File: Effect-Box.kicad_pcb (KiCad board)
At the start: 6 copper layers, 178.6 x 140 mm, 161 parts, among them J1 Conn_02x07_Odd_Even, J10 Power pins, J2 26642801RP2, J3 FH12A-10S-0.5SH55, J5 Conn_ARM_JTAG_SWD_20, J6 26642801RP2, J7 AudioJack3, J8 AudioJack3, J9 PJ-006A-SMT, SW0 SW_Push, SW1 SW_Push, SW2 SW_Push, SW3 SW_Push, SW4 SW_Push, SW5 SW_Push, SW6 SW_Push, U1 TPS54325, U10 LM7805SX_NOPB, U2 TPS54294, U3 XC7A100T-FTG256, U4 S25FL1, U5 SiT2024B, U7 EFM32GG942F1024, U8 INA1651IPW, U9 PCM3003E

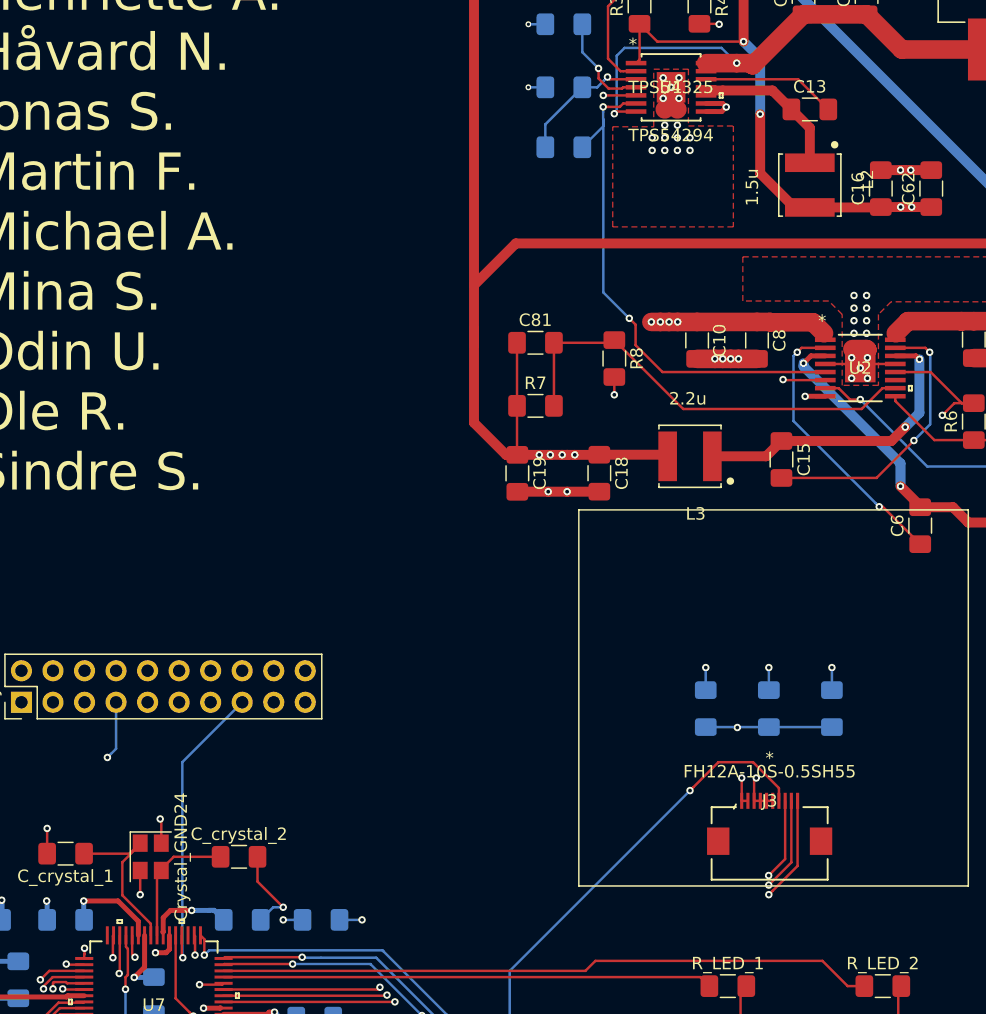
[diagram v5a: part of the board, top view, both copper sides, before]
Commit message: Fix more silkscreen and reimport from schematic
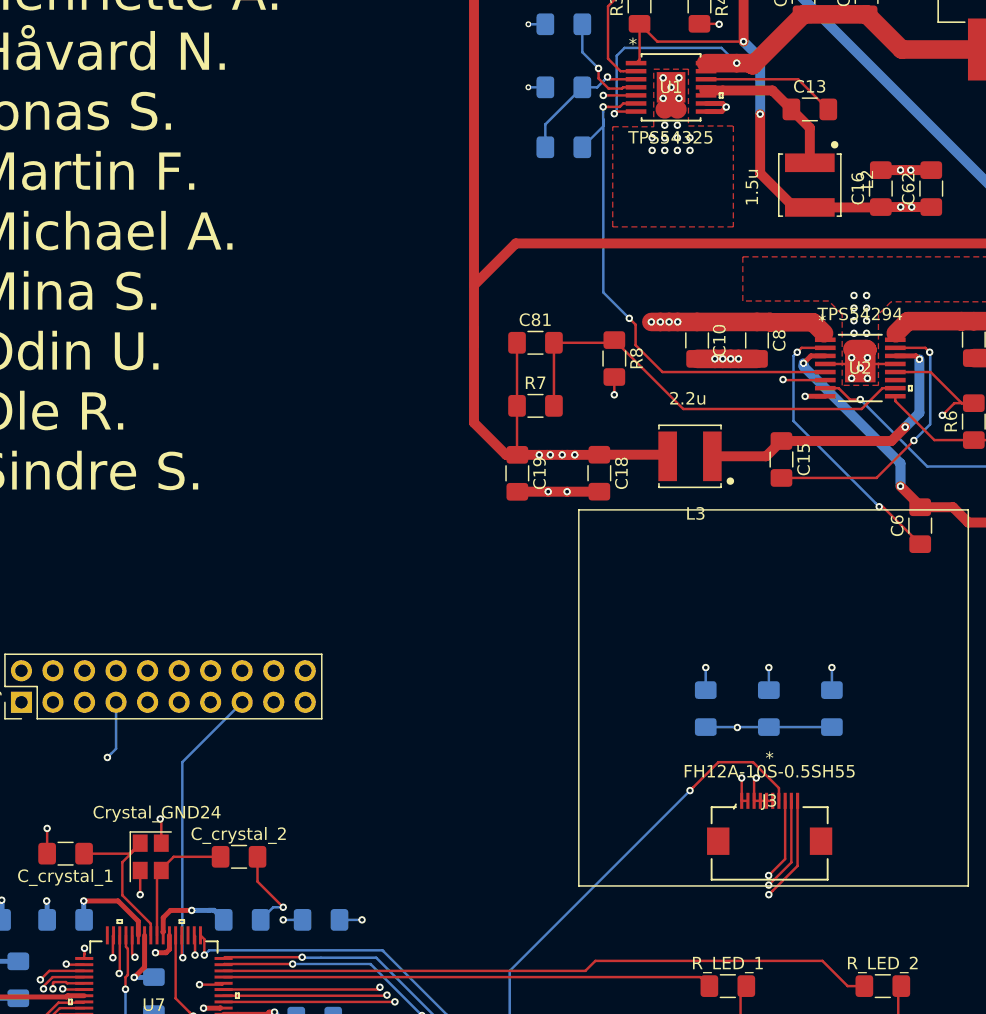
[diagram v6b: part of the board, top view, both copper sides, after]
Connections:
- J1 pad 12: (no net) -> Net-(J1-Pad12)
- J1 pad 14: (no net) -> Net-(J1-Pad14)
- J2 pad 17: (no net) -> Net-(J2-Pad17)
- J2 pad 18: (no net) -> Net-(J2-Pad18)
- J2 pad 19: (no net) -> Net-(J2-Pad19)
- J2 pad 20: (no net) -> Net-(J2-Pad20)
- J2 pad 21: (no net) -> Net-(J2-Pad21)
- J2 pad 22: (no net) -> Net-(J2-Pad22)
- J2 pad 23: (no net) -> Net-(J2-Pad23)
- J2 pad 24: (no net) -> Net-(J2-Pad24)
- J2 pad 25: (no net) -> Net-(J2-Pad25)
- J2 pad 26: (no net) -> Net-(J2-Pad26)
- J3 pad 11: (no net) -> Net-(J3-Pad11)
- J3 pad 12: (no net) -> Net-(J3-Pad12)
- J5 pad 11: (no net) -> Net-(J5-Pad11)
- J5 pad 17: (no net) -> Net-(J5-Pad17)
- J5 pad 19: (no net) -> Net-(J5-Pad19)
- J5 pad 2: (no net) -> Net-(J5-Pad2)
- J5 pad 3: (no net) -> Net-(J5-Pad3)
- J5 pad 5: (no net) -> Net-(J5-Pad5)
- J9 pad 3: (no net) -> Net-(J9-Pad3)
- U2 pad 11: (no net) -> Net-(U2-Pad11)
- U3 pad A10: (no net) -> Net-(U3-PadA10)
- U3 pad A12: (no net) -> Net-(U3-PadA12)
- U3 pad A13: (no net) -> Net-(U3-PadA13)
- U3 pad A14: (no net) -> Net-(U3-PadA14)
- U3 pad A15: (no net) -> Net-(U3-PadA15)
- U3 pad A2: (no net) -> Net-(U3-PadA2)
- U3 pad A3: (no net) -> Net-(U3-PadA3)
- U3 pad A4: (no net) -> Net-(U3-PadA4)
- U3 pad A5: (no net) -> Net-(U3-PadA5)
- U3 pad A7: (no net) -> Net-(U3-PadA7)
- U3 pad A8: (no net) -> Net-(U3-PadA8)
- U3 pad A9: (no net) -> Net-(U3-PadA9)
- U3 pad B1: (no net) -> Net-(U3-PadB1)
- U3 pad B10: (no net) -> Net-(U3-PadB10)
- U3 pad B11: (no net) -> Net-(U3-PadB11)
- U3 pad B12: (no net) -> Net-(U3-PadB12)
- U3 pad B14: (no net) -> Net-(U3-PadB14)
- U3 pad B15: (no net) -> Net-(U3-PadB15)
- U3 pad B16: (no net) -> Net-(U3-PadB16)
- U3 pad B2: (no net) -> Net-(U3-PadB2)
- U3 pad B4: (no net) -> Net-(U3-PadB4)
- U3 pad B5: (no net) -> Net-(U3-PadB5)
- U3 pad B6: (no net) -> Net-(U3-PadB6)
- U3 pad B7: (no net) -> Net-(U3-PadB7)
- U3 pad B9: (no net) -> Net-(U3-PadB9)
- U3 pad C1: (no net) -> Net-(U3-PadC1)
- U3 pad C11: (no net) -> Net-(U3-PadC11)
- U3 pad C12: (no net) -> Net-(U3-PadC12)
- U3 pad C13: (no net) -> Net-(U3-PadC13)
- U3 pad C14: (no net) -> Net-(U3-PadC14)
- U3 pad C16: (no net) -> Net-(U3-PadC16)
- U3 pad C2: (no net) -> Net-(U3-PadC2)
- U3 pad C3: (no net) -> Net-(U3-PadC3)
- U3 pad C4: (no net) -> Net-(U3-PadC4)
- U3 pad C6: (no net) -> Net-(U3-PadC6)
- U3 pad C7: (no net) -> Net-(U3-PadC7)
- U3 pad C8: (no net) -> Net-(U3-PadC8)
- U3 pad C9: (no net) -> Net-(U3-PadC9)
- U3 pad D1: (no net) -> Net-(U3-PadD1)
- U3 pad D10: (no net) -> Net-(U3-PadD10)
- U3 pad D11: (no net) -> Net-(U3-PadD11)
- U3 pad D13: (no net) -> Net-(U3-PadD13)
- U3 pad D14: (no net) -> Net-(U3-PadD14)
- U3 pad D15: (no net) -> Net-(U3-PadD15)
- U3 pad D16: (no net) -> Net-(U3-PadD16)
- U3 pad D3: (no net) -> Net-(U3-PadD3)
- U3 pad D4: (no net) -> Net-(U3-PadD4)
- U3 pad D5: (no net) -> Net-(U3-PadD5)
- U3 pad D6: (no net) -> Net-(U3-PadD6)
- U3 pad D8: (no net) -> Net-(U3-PadD8)
- U3 pad D9: (no net) -> Net-(U3-PadD9)
- U3 pad E1: (no net) -> Net-(U3-PadE1)
- U3 pad E11: (no net) -> Net-(U3-PadE11)
- U3 pad E12: (no net) -> Net-(U3-PadE12)
- U3 pad E13: (no net) -> Net-(U3-PadE13)
- U3 pad E15: (no net) -> Net-(U3-PadE15)
- U3 pad E16: (no net) -> Net-(U3-PadE16)
- U3 pad E2: (no net) -> Net-(U3-PadE2)
- U3 pad E3: (no net) -> Net-(U3-PadE3)
- U3 pad E5: (no net) -> Net-(U3-PadE5)
- U3 pad E6: (no net) -> Net-(U3-PadE6)
- U3 pad F12: (no net) -> Net-(U3-PadF12)
- U3 pad F13: (no net) -> Net-(U3-PadF13)
- U3 pad F14: (no net) -> Net-(U3-PadF14)
- U3 pad F15: (no net) -> Net-(U3-PadF15)
- U3 pad F2: (no net) -> Net-(U3-PadF2)
- U3 pad F3: (no net) -> Net-(U3-PadF3)
- U3 pad F4: (no net) -> Net-(U3-PadF4)
- U3 pad F5: (no net) -> Net-(U3-PadF5)
- U3 pad G1: (no net) -> Net-(U3-PadG1)
- U3 pad G11: (no net) -> Net-(U3-PadG11)
- U3 pad G12: (no net) -> Net-(U3-PadG12)
- U3 pad G14: (no net) -> Net-(U3-PadG14)
- U3 pad G15: (no net) -> Net-(U3-PadG15)
- U3 pad G16: (no net) -> Net-(U3-PadG16)
- U3 pad G2: (no net) -> Net-(U3-PadG2)
- U3 pad G4: (no net) -> Net-(U3-PadG4)
- U3 pad G5: (no net) -> Net-(U3-PadG5)
- U3 pad H1: (no net) -> Net-(U3-PadH1)
- U3 pad H11: (no net) -> Net-(U3-PadH11)
- U3 pad H12: (no net) -> Net-(U3-PadH12)
- U3 pad H13: (no net) -> Net-(U3-PadH13)
- U3 pad H14: (no net) -> Net-(U3-PadH14)
- U3 pad H16: (no net) -> Net-(U3-PadH16)
- U3 pad H2: (no net) -> Net-(U3-PadH2)
- U3 pad H3: (no net) -> Net-(U3-PadH3)
- U3 pad H4: (no net) -> Net-(U3-PadH4)
- U3 pad H5: (no net) -> Net-(U3-PadH5)
- U3 pad J1: (no net) -> Net-(U3-PadJ1)
- U3 pad J15: (no net) -> Net-(U3-PadJ15)
- U3 pad J16: (no net) -> Net-(U3-PadJ16)
- U3 pad J3: (no net) -> Net-(U3-PadJ3)
- U3 pad J4: (no net) -> Net-(U3-PadJ4)
- U3 pad J5: (no net) -> Net-(U3-PadJ5)
- U3 pad K1: (no net) -> Net-(U3-PadK1)
- U3 pad K12: (no net) -> Net-(U3-PadK12)
- U3 pad K2: (no net) -> Net-(U3-PadK2)
- U3 pad K3: (no net) -> Net-(U3-PadK3)
- U3 pad K5: (no net) -> Net-(U3-PadK5)
- U3 pad K7: (no net) -> Net-(U3-PadK7)
- U3 pad K8: (no net) -> Net-(U3-PadK8)
- U3 pad L13: (no net) -> Net-(U3-PadL13)
- U3 pad L2: (no net) -> Net-(U3-PadL2)
- U3 pad L3: (no net) -> Net-(U3-PadL3)
- U3 pad L4: (no net) -> Net-(U3-PadL4)
- U3 pad L5: (no net) -> Net-(U3-PadL5)
- U3 pad M1: (no net) -> Net-(U3-PadM1)
- U3 pad M2: (no net) -> Net-(U3-PadM2)
- U3 pad M4: (no net) -> Net-(U3-PadM4)
- U3 pad M5: (no net) -> Net-(U3-PadM5)
- U3 pad N1: (no net) -> Net-(U3-PadN1)
- U3 pad N13: (no net) -> Net-(U3-PadN13)
- U3 pad N2: (no net) -> Net-(U3-PadN2)
- U3 pad N3: (no net) -> Net-(U3-PadN3)
- U3 pad N4: (no net) -> Net-(U3-PadN4)
- U3 pad P1: (no net) -> Net-(U3-PadP1)
- U3 pad P13: (no net) -> Net-(U3-PadP13)
- U3 pad P3: (no net) -> Net-(U3-PadP3)
- U3 pad P4: (no net) -> Net-(U3-PadP4)
- U3 pad P5: (no net) -> Net-(U3-PadP5)
- U3 pad P6: (no net) -> Net-(U3-PadP6)
- U3 pad R1: (no net) -> Net-(U3-PadR1)
- U3 pad R2: (no net) -> Net-(U3-PadR2)
- U3 pad R3: (no net) -> Net-(U3-PadR3)
- U3 pad R5: (no net) -> Net-(U3-PadR5)
- U3 pad R6: (no net) -> Net-(U3-PadR6)
- U3 pad R7: (no net) -> Net-(U3-PadR7)
- U3 pad R8: (no net) -> Net-(U3-PadR8)
- U3 pad T10: (no net) -> Net-(U3-PadT10)
- U3 pad T15: (no net) -> Net-(U3-PadT15)
- U3 pad T2: (no net) -> Net-(U3-PadT2)
- U3 pad T3: (no net) -> Net-(U3-PadT3)
- U3 pad T4: (no net) -> Net-(U3-PadT4)
- U3 pad T5: (no net) -> Net-(U3-PadT5)
- U3 pad T7: (no net) -> Net-(U3-PadT7)
- U3 pad T8: (no net) -> Net-(U3-PadT8)
- U3 pad T9: (no net) -> Net-(U3-PadT9)
- U5 pad 2: (no net) -> Net-(U5-Pad2)
- U7 pad 19: (no net) -> Net-(U7-Pad19)
- U7 pad 32: (no net) -> Net-(U7-Pad32)
- U8 pad 5: (no net) -> Net-(U8-Pad5)
- U8 pad 6: (no net) -> Net-(U8-Pad6)
- U8 pad 7: (no net) -> Net-(U8-Pad7)
- U8 pad 8: (no net) -> Net-(U8-Pad8)
- U8 pad 9: (no net) -> Net-(U8-Pad9)
- U9 pad 16: (no net) -> Net-(U9-Pad16)

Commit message: Move enev more silkscreen
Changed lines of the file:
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@@
-(kicad_pcb (version 20171130) (host pcbnew "(5.1.4)-1")
+(kicad_pcb (version 20171130) (host pcbnew 5.1.4-e60b266~84~ubuntu19.04.1)
   (general
     (thickness 1.6)
@@
   (module Local:FH12A-10S-0.5SH55 (layer F.Cu)
     (at 164.9095 94.1705 180)
-    (fp_text reference J3 (at 0 -3.429) (layer F.SilkS)
+    (fp_text reference J3 (at -4.0005 -2.6035) (layer F.SilkS)
       (effects (font (size 1 1) (thickness 0.15)))
     )

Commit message: Move some silk again
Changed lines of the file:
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@@
   (page A4)
   (layers
-    (0 F.Cu signal)
+    (0 F.Cu signal hide)
     (1 VCC.Cu power hide)
     (2 In1.Cu signal hide)
@@
     (36 B.SilkS user)
     (37 F.SilkS user)
-    (38 B.Mask user hide)
-    (39 F.Mask user hide)
-    (40 Dwgs.User user hide)
-    (41 Cmts.User user hide)
-    (42 Eco1.User user hide)
-    (43 Eco2.User user hide)
-    (44 Edge.Cuts user hide)
-    (45 Margin user hide)
-    (46 B.CrtYd user hide)
-    (47 F.CrtYd user hide)
-    (48 B.Fab user hide)
-    (49 F.Fab user hide)
+    (38 B.Mask user)
+    (39 F.Mask user)
+    (40 Dwgs.User user)
+    (41 Cmts.User user)
+    (42 Eco1.User user)
+    (43 Eco2.User user)
+    (44 Edge.Cuts user)
+    (45 Margin user)
+    (46 B.CrtYd user)
+    (47 F.CrtYd user)
+    (48 B.Fab user)
+    (49 F.Fab user)
   )
   (setup
@@
       (effects (font (size 1 1) (thickness 0.15)))
     )
-    (fp_text value 26642801RP2 (at 1.27 35.35 90) (layer F.Fab)
+    (fp_text value 26642801RP2 (at -3.1115 16.51 180) (layer F.Fab)
       (effects (font (size 1 1) (thickness 0.15)))
     )
@@
       (effects (font (size 1 1) (thickness 0.15)))
     )
-    (fp_text value Conn_02x07_Odd_Even (at 1 14.06 90) (layer F.Fab)
+    (fp_text value Conn_02x07_Odd_Even (at 4.826 5.715 180) (layer F.Fab)
       (effects (font (size 1 1) (thickness 0.15)))
     )
@@
       (effects (font (size 1 1) (thickness 0.15)))
     )
-    (fp_text value "Power pins" (at 0 20.11 90) (layer F.Fab)
+    (fp_text value "Power pins" (at 2.9845 9.144 180) (layer F.Fab)
       (effects (font (size 1 1) (thickness 0.15)))
     )
@@
     (at 168.148 48.006 270)
     (attr smd)
-    (fp_text reference L2 (at -0.46027 -4.63772 90) (layer F.SilkS)
+    (fp_text reference L2 (at 0.0635 6.223 90) (layer F.SilkS)
       (effects (font (size 1.00059 1.00059) (thickness 0.05)))
     )
@@
     (at 183.134 37.084 90)
     (attr smd)
-    (fp_text reference J9 (at 4.89039 -8.10565 90) (layer F.SilkS)
+    (fp_text reference J9 (at 6.7945 -5.5245 90) (layer F.SilkS)
       (effects (font (size 1.00008 1.00008) (thickness 0.05)))
     )
-    (fp_text value PJ-006A-SMT (at 5.02762 11.0208 90) (layer F.SilkS)
+    (fp_text value PJ-006A-SMT (at 7.6835 10.922 90) (layer F.SilkS)
       (effects (font (size 1.00052 1.00052) (thickness 0.05)))
     )
@@
       (effects (font (size 1 1) (thickness 0.15)))
     )
-    (fp_text value Conn_ARM_JTAG_SWD_20 (at 1.27 25.19 90) (layer F.Fab)
+    (fp_text value Conn_ARM_JTAG_SWD_20 (at 6.1595 12.1285 180) (layer F.Fab)
       (effects (font (size 1 1) (thickness 0.15)))
     )
@@
       (effects (font (size 1 1) (thickness 0.15)))
     )
-    (fp_text value 26642801RP2 (at 1.27 35.35) (layer F.Fab)
+    (fp_text value 26642801RP2 (at -2.8575 17.0815 270) (layer F.Fab)
       (effects (font (size 1 1) (thickness 0.15)))
     )
